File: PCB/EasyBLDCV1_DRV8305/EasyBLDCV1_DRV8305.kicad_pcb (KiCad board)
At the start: 4 copper layers, 82.2 x 60.3 mm, 73 parts, among them J1 10159560-A00221RLF, J2 TC2050-IDC, Q1 CSD16556Q5B, Q2 CSD16556Q5B, Q3 CSD16556Q5B, Q4 CSD16556Q5B, Q5 CSD16556Q5B, Q6 CSD16556Q5B, U1 DRV83053PHP, U2 TMS320F28027FPTT, U3 TPD4E05U06DQAR, U4 LMR16006XDDCR

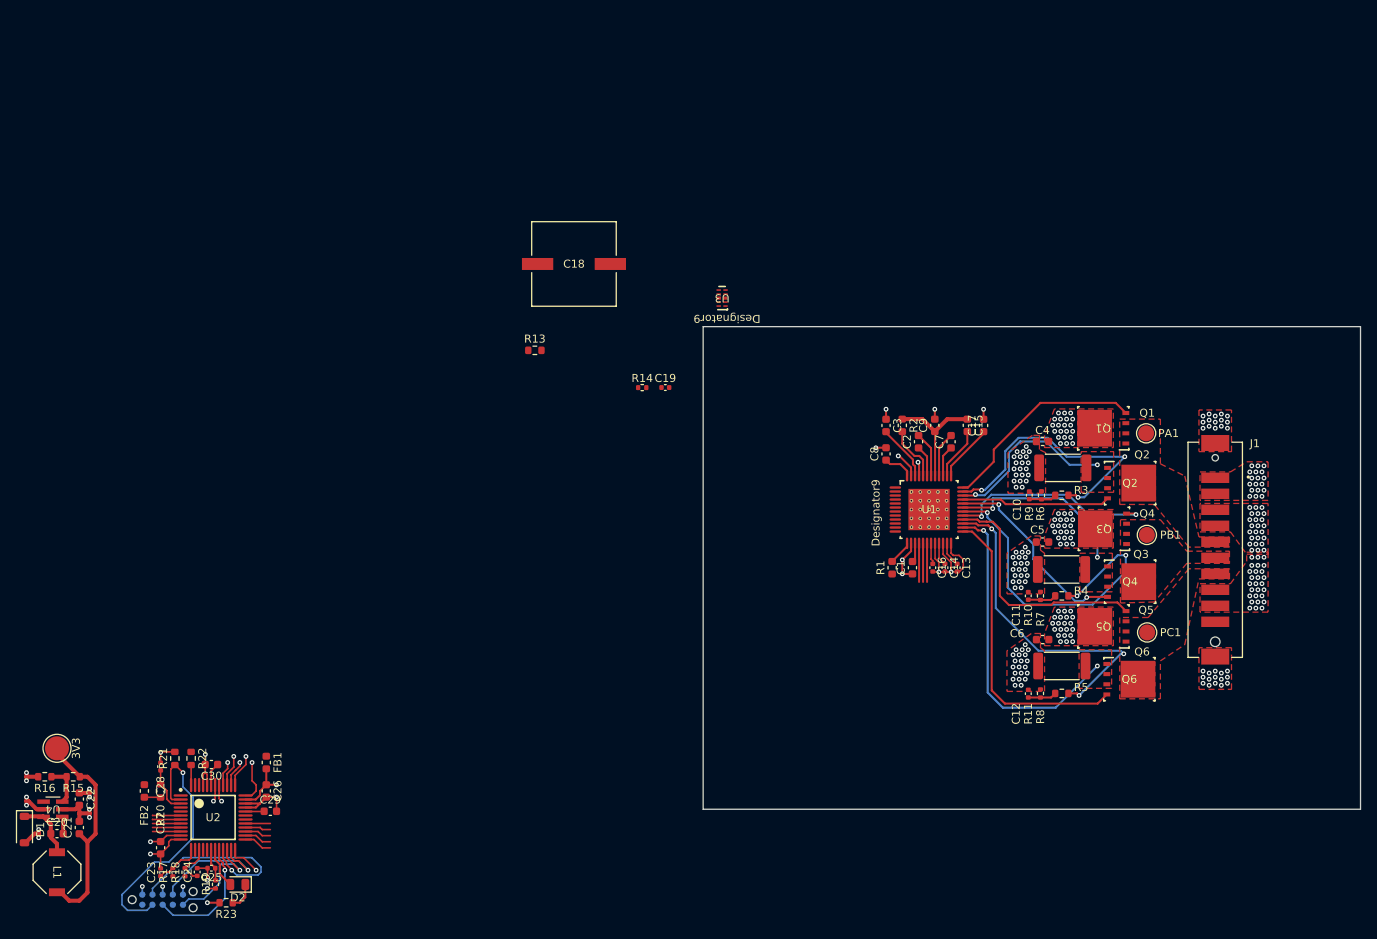
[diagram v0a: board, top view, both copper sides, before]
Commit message: Started Connecting Microcontroller
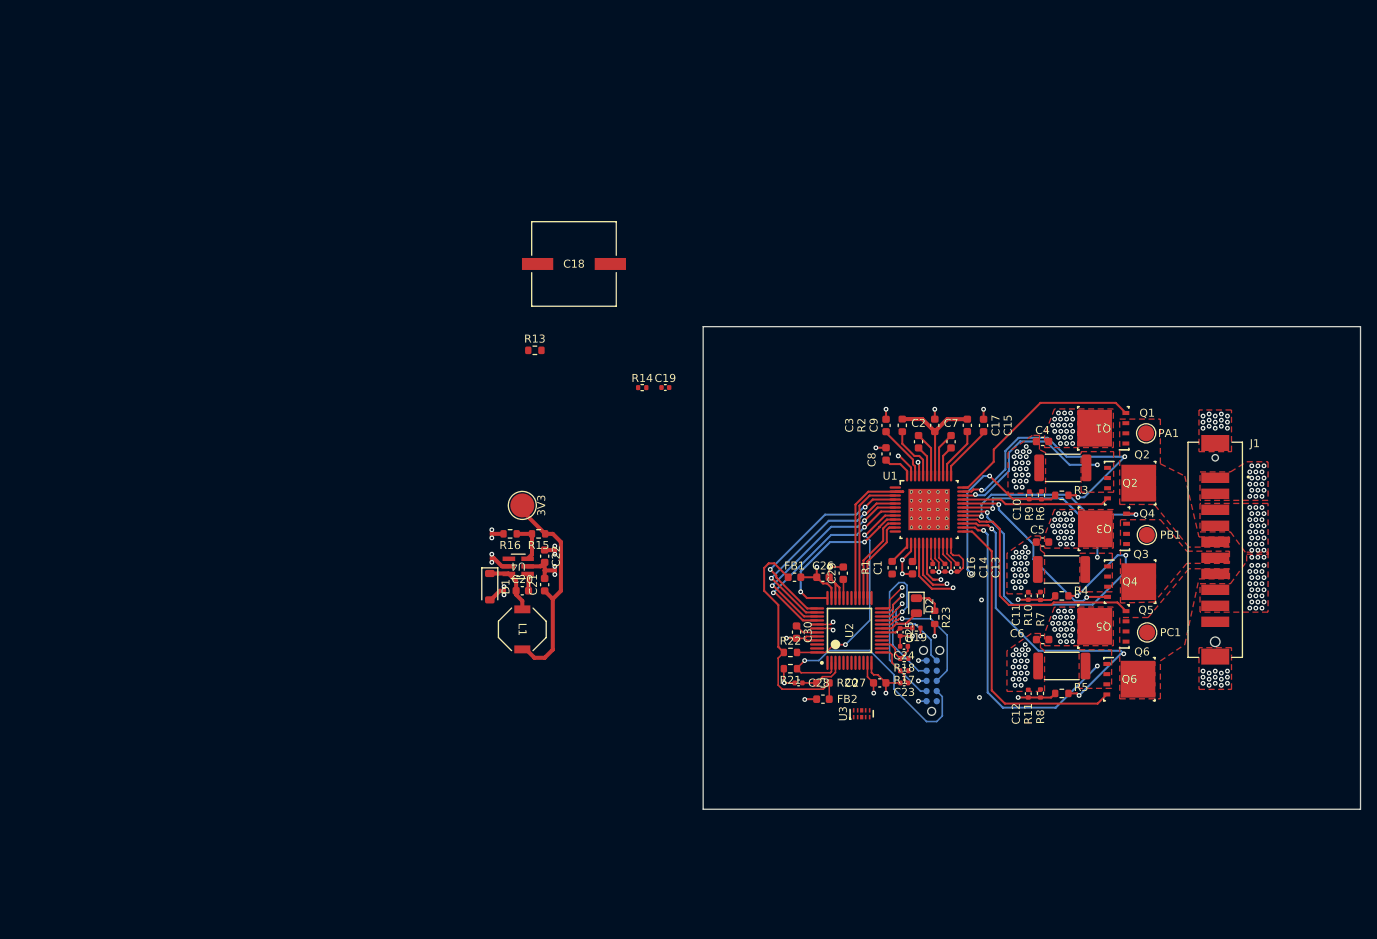
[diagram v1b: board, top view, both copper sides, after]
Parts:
- moved J2 99.9 mm to (204.6, 161.0), turned to 90 degrees
- moved C23 95.9 mm to (201.2, 161.2), turned to 180 degrees
- moved R23 95.5 mm to (205.0, 153.1), turned to -90 degrees
- moved R17 94.8 mm to (201.2, 159.7), turned to 180 degrees
- moved R18 93.8 mm to (201.2, 158.2), turned to 180 degrees
- moved R19 93.3 mm to (202.7, 154.4), turned to 180 degrees
- moved C24 92.7 mm to (201.1, 156.7), turned to 180 degrees
- moved C27 92.2 mm to (198.1, 161.2), turned to 0 degrees
- moved D2 91.7 mm to (202.7, 151.6), turned to -90 degrees
- moved C25 91.0 mm to (200.6, 154.9), turned to -90 degrees
- moved FB2 85.6 mm to (191.0, 163.3), turned to 180 degrees
- moved R20 83.9 mm to (191.0, 161.2), turned to 180 degrees
- moved U2 82.9 mm to (194.3, 154.7), turned to 90 degrees
- moved C28 80.4 mm to (187.9, 161.2), turned to 180 degrees
- moved R21 77.8 mm to (186.9, 159.5), turned to 180 degrees
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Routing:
- net 3.3V: track 34.0 -> 60.8 mm
- net nFAULT: track 2.50 -> 26.5 mm, vias 0 -> 2
- net INL_B: track 3.28 -> 26.9 mm, vias 1 -> 2
- net INL_C: track 3.06 -> 26.4 mm, vias 1 -> 2
- net INH_B: track 4.15 -> 27.3 mm, vias 1 -> 2
- net INH_C: track 3.93 -> 26.6 mm, vias 1 -> 2
- net VSEN_A: track 7.00 -> 23.6 mm, vias 0 -> 2
- net INH_A: track 3.10 -> 19.3 mm
- net nSCS: track 5.33 -> 20.7 mm, vias 1 -> 2
- net INL_A: track 3.21 -> 16.5 mm
- net SDI: track 3.32 -> 11.5 mm
- net SDO: track 3.43 -> 10.7 mm
- net ISEN_A: track 4.83 -> 9.05 mm, vias 0 -> 1
- net COM: track 3.54 -> 0.00 mm
- net unconnected-(U2-ADCINA2_COMP1A_AIO2-Pad9): track 3.52 -> 0.00 mm
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
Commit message: Continued layout work
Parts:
- added COM1: TestPoint, TestPoint:TestPoint_Pad_D2.0mm, F.Cu at (169.9, 115.2)
- moved U3 82.5 mm to (129.0, 116.7)
- moved C16 80.6 mm to (138.9, 100.3)
- moved C2 80.6 mm to (137.2, 84.5)
- moved C23 80.6 mm to (135.4, 114.7)
- moved C26 80.6 mm to (125.2, 101.5)
- moved C27 80.6 mm to (132.3, 114.7)
- moved C28 80.6 mm to (122.2, 114.7)
- moved C7 80.6 mm to (141.2, 84.5)
- moved C8 80.6 mm to (133.1, 86.1)
- moved FB1 80.6 mm to (121.6, 101.5)
- moved Q1 80.6 mm to (160.2, 82.9)
- moved Q6 80.6 mm to (163.5, 114.2)
- moved R17 80.6 mm to (135.4, 113.2)
- moved R2 80.6 mm to (135.1, 82.5)
- moved R20 80.6 mm to (125.2, 114.7)
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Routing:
- net WAKE: track 5.32 -> 33.6 mm
- net EN_GATE: track 2.13 -> 24.2 mm, vias 1 -> 2
- net ISEN_B: track 7.49 -> 24.4 mm, vias 1 -> 2
- net SL_B: track 25.8 -> 42.6 mm, vias 2 -> 3
- net ISEN_A: track 9.05 -> 24.6 mm
- net ISEN_C: track 6.85 -> 18.6 mm, vias 2 -> 3
- net SL_A: track 25.3 -> 36.7 mm, vias 2 -> 3
- net SL_C: track 42.5 -> 52.1 mm, vias 2 -> 3
- net VSEN_PVDD: track 0.00 -> 3.47 mm, vias 0 -> 1
- net VSEN_A: track 23.6 -> 21.9 mm
- net VDDIO: track 6.93 -> 5.66 mm, vias 1 -> 0
- net GND: track 71.6 -> 70.8 mm
- net PVDD: track 21.0 -> 21.1 mm, vias 85 -> 101
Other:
- board size 82.2 x 60.3 mm -> 77.6 x 42 mm

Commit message: Finished Initial Layout
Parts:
- 3V3: footprint TestPoint:TestPoint_Pad_D3.0mm -> TestPoint:TestPoint_Pad_D2.0mm
- C18: value 390u -> 10u; footprint EasyBLDC:CAP_FP_10P3X10P3_PAN -> Capacitor_SMD:C_1210_3225Metric
- moved C18 70.3 mm to (179.8, 91.9)
- moved R13 23.3 mm to (119.1, 117.3), turned to -90 degrees
- moved R14 21.4 mm to (120.9, 117.9), turned to 90 degrees
- moved C19 20.5 mm to (122.3, 117.9), turned to 90 degrees
- moved L1 12.4 mm to (122.2, 91.6), turned to -90 degrees
- moved C21 9.47 mm to (125.0, 86.0), turned to 90 degrees
- moved R15 9.44 mm to (124.2, 79.6), turned to 180 degrees
- moved C22 8.92 mm to (125.0, 82.4), turned to -90 degrees
- moved C20 6.68 mm to (122.2, 86.7), turned to 0 degrees
- moved R16 6.08 mm to (120.7, 79.6), turned to 180 degrees
- moved U4 4.13 mm to (121.7, 83.7), turned to 180 degrees
- moved D1 3.99 mm to (118.1, 86.2), turned to -90 degrees
- moved 3V3 2.87 mm to (129.0, 87.0), turned to 0 degrees
- moved COM1 0.45 mm to (169.8, 114.8)
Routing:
- net COM: track 0.00 -> 110.7 mm, vias 0 -> 2
- net 3.3V: track 60.8 -> 108.1 mm, vias 1 -> 4
- net VSEN_A: track 21.9 -> 66.8 mm
- net VSEN_B: track 9.46 -> 41.7 mm
- net VSEN_C: track 9.67 -> 38.6 mm, vias 2 -> 4
- net VSEN_PVDD: track 3.47 -> 24.7 mm, vias 1 -> 3
- net VDDA: track 5.61 -> 15.7 mm
- net SCLK: track 4.18 -> 13.0 mm, vias 1 -> 0
- net GND: track 70.8 -> 74.9 mm, vias 167 -> 162
- net TCK: track 15.9 -> 17.4 mm
- net PVDD: track 21.1 -> 22.4 mm, vias 101 -> 93
- net nSCS: track 20.7 -> 19.5 mm
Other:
- board size 77.6 x 42 mm -> 66.4 x 43.1 mm
